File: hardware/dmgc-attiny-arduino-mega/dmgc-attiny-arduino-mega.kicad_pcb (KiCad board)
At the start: 2 copper layers, 101.6 x 53.3 mm, 34 parts, among them J1 Power, J2 PWM, J3 Analog, J4 PWM, J5 Analog, J6 Communication, J7 Digital, SW1 PUSH, SW2 LEFT, SW3 RIGHT, SW4 SELECT, SW5 START/RESET, U1 ATtiny85-20P

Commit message: Updated arduino shield, start implementing a multiplexer to switch from flashing the attiny85 to running the attiny85.
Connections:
- D8 pad 4: unconnected-(D8-Pad4) -> GND
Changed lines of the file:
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@@
   (net 85 "Net-(D6-Pad4)")
   (net 86 "Net-(D7-Pad4)")
-  (net 87 "unconnected-(D8-Pad4)")
+  (net 87 "Net-(U1-Pad1)")
   (net 88 "Net-(R1-Pad2)")
   (net 89 "Net-(R2-Pad2)")
@@
   (net 96 "Net-(SW4-Pad1)")
   (net 97 "Net-(SW5-Pad1)")
-  (net 98 "Net-(R6-Pad2)")
-  (net 99 "unconnected-(SW1-Pad4)")
-  (net 100 "unconnected-(SW2-Pad4)")
-  (net 101 "unconnected-(SW3-Pad4)")
-  (net 102 "unconnected-(SW4-Pad4)")
-  (net 103 "unconnected-(SW5-Pad4)")
+  (net 98 "unconnected-(SW1-Pad4)")
+  (net 99 "unconnected-(SW2-Pad4)")
+  (net 100 "unconnected-(SW3-Pad4)")
+  (net 101 "unconnected-(SW4-Pad4)")
+  (net 102 "unconnected-(SW5-Pad4)")
   (footprint "Connector_PinSocket_2.54mm:PinSocket_2x18_P2.54mm_Vertical" locked (layer "F.Cu")
     (at 193.98 92.38 180)
@@
       (effects (font (size 1 1) (thickness 0.15)))
     )
+    (fp_line (start -3.87 -1.33) (end -3.868838 43.122722) (layer "F.SilkS") (width 0.12))
     (fp_line (start -1.27 -1.33) (end -1.27 1.27) (layer "F.SilkS") (width 0.12))
     (fp_line (start 1.33 1.27) (end 1.33 44.51) (layer "F.SilkS") (width 0.12))
@@
     (fp_line (start -1.27 1.27) (end 1.33 1.27) (layer "F.SilkS") (width 0.12))
     (fp_line (start 1.33 -1.33) (end 1.33 0) (layer "F.SilkS") (width 0.12))
-    (fp_line (start -3.87 44.51) (end 1.33 44.51) (layer "F.SilkS") (width 0.12))
     (fp_line (start -3.87 -1.33) (end -1.27 -1.33) (layer "F.SilkS") (width 0.12))
-    (fp_line (start -3.87 -1.33) (end -3.87 44.51) (layer "F.SilkS") (width 0.12))
+    (fp_line (start 1.33 44.51) (end -2.536649 44.510068) (layer "F.SilkS") (width 0.12))
+    (fp_arc (start -2.536649 44.510068) (mid -3.499381 44.101239) (end -3.868838 43.122722) (layer "F.SilkS") (width 0.12))
     (fp_line (start -4.34 -1.8) (end 1.76 -1.8) (layer "F.CrtYd") (width 0.05))
     (fp_line (start -4.34 44.95) (end -4.34 -1.8) (layer "F.CrtYd") (width 0.05))
@@
       (net 1 "GND") (pinfunction "3") (pintype "passive"))
     (pad "4" thru_hole circle (at 6.5 4.5 90) (size 2 2) (drill 1.1) (layers *.Cu *.Mask)
-      (net 100 "unconnected-(SW2-Pad4)") (pinfunction "4") (pintype "passive"))
+      (net 99 "unconnected-(SW2-Pad4)") (pinfunction "4") (pintype "passive"))
     (model "${KICAD6_3DMODEL_DIR}/Button_Switch_THT.3dshapes/SW_PUSH_6mm.wrl"
       (offset (xyz 0 0 0))
@@
       (net 1 "GND") (pinfunction "3") (pintype "passive"))
     (pad "4" thru_hole circle (at 6.5 4.5 90) (size 2 2) (drill 1.1) (layers *.Cu *.Mask)
-      (net 99 "unconnected-(SW1-Pad4)") (pinfunction "4") (pintype "passive"))
+      (net 98 "unconnected-(SW1-Pad4)") (pinfunction "4") (pintype "passive"))
     (model "${KICAD6_3DMODEL_DIR}/Button_Switch_THT.3dshapes/SW_PUSH_6mm.wrl"
       (offset (xyz 0 0 0))
@@
       (net 1 "GND") (pinfunction "3") (pintype "passive"))
     (pad "4" thru_hole circle (at 6.5 4.5 90) (size 2 2) (drill 1.1) (layers *.Cu *.Mask)
-      (net 102 "unconnected-(SW4-Pad4)") (pinfunction "4") (pintype "passive"))
+      (net 101 "unconnected-(SW4-Pad4)") (pinfunction "4") (pintype "passive"))
     (model "${KICAD6_3DMODEL_DIR}/Button_Switch_THT.3dshapes/SW_PUSH_6mm.wrl"
       (offset (xyz 0 0 0))
@@
       (net 1 "GND") (pinfunction "3") (pintype "passive"))
     (pad "4" thru_hole circle (at 6.5 4.5 90) (size 2 2) (drill 1.1) (layers *.Cu *.Mask)
-      (net 103 "unconnected-(SW5-Pad4)") (pinfunction "4") (pintype "passive"))
+      (net 102 "unconnected-(SW5-Pad4)") (pinfunction "4") (pintype "passive"))
     (model "${KICAD6_3DMODEL_DIR}/Button_Switch_THT.3dshapes/SW_PUSH_6mm.wrl"
       (offset (xyz 0 0 0))
@@
       (net 1 "GND") (pinfunction "3") (pintype "passive"))
     (pad "4" thru_hole circle (at 6.5 4.5 90) (size 2 2) (drill 1.1) (layers *.Cu *.Mask)
-      (net 101 "unconnected-(SW3-Pad4)") (pinfunction "4") (pintype "passive"))
+      (net 100 "unconnected-(SW3-Pad4)") (pinfunction "4") (pintype "passive"))
     (model "${KICAD6_3DMODEL_DIR}/Button_Switch_THT.3dshapes/SW_PUSH_6mm.wrl"
       (offset (xyz 0 0 0))
@@
       (net 79 "Net-(D1-Pad2)") (pintype "passive"))
     (pad "2" smd roundrect (at 0.32 0 270) (size 0.46 0.4) (layers "F.Cu" "F.Mask") (roundrect_rratio 0.25)
-      (net 98 "Net-(R6-Pad2)") (pintype "passive"))
+      (net 87 "Net-(U1-Pad1)") (pintype "passive"))
     (model "${KICAD6_3DMODEL_DIR}/Resistor_SMD.3dshapes/R_0201_0603Metric.wrl"
       (offset (xyz 0 0 0))
@@
     (fp_line (start 0.635 8.89) (end 0.635 -0.27) (layer "F.Fab") (width 0.1))
     (pad "1" thru_hole rect (at 0 0) (size 1.6 1.6) (drill 0.8) (layers *.Cu *.Mask)
-      (net 98 "Net-(R6-Pad2)") (pinfunction "~{RESET}/PB5") (pintype "bidirectional"))
+      (net 87 "Net-(U1-Pad1)") (pinfunction "~{RESET}/PB5") (pintype "bidirectional"))
     (pad "2" thru_hole oval (at 0 2.54) (size 1.6 1.6) (drill 0.8) (layers *.Cu *.Mask)
       (net 96 "Net-(SW4-Pad1)") (pinfunction "XTAL1/PB3") (pintype "bidirectional"))
@@
       (net 34 "+5V") (pinfunction "VDD") (pintype "power_in"))
     (pad "4" smd rect (at 2.45 -1.6) (size 1.5 1) (layers "F.Cu" "F.Paste" "F.Mask")
-      (net 87 "unconnected-(D8-Pad4)") (pinfunction "DO") (pintype "output"))
+      (net 1 "GND") (pinfunction "DO") (pintype "output"))
     (model "${KICAD6_3DMODEL_DIR}/LED_SMD.3dshapes/LED_Inolux_IN-PI554FCH_PLCC4_5.0x5.0mm_P3.2mm.wrl"
       (offset (xyz 0 0 0))
@@
   (segment (start 161.53 60.02) (end 160.87 59.36) (width 0.25) (layer "F.Cu") (net 86))
   (segment (start 168.76 60.02) (end 161.53 60.02) (width 0.25) (layer "F.Cu") (net 86))
+  (segment (start 174.94 64.652231) (end 174.948637 64.643594) (width 0.25) (layer "F.Cu") (net 87))
+  (segment (start 174.94 68.26) (end 174.94 64.652231) (width 0.25) (layer "F.Cu") (net 87))
   (segment (start 136.27 85.98591) (end 136.27 87.59) (width 0.25) (layer "F.Cu") (net 88))
   (segment (start 137.25269 85.00322) (end 136.27 85.98591) (width 0.25) (layer "F.Cu") (net 88))
@@
   (segment (start 176.528198 69.848198) (end 181.525606 64.85079) (width 0.25) (layer "F.Cu") (net 97))
   (segment (start 188.45 64.94522) (end 188.45 84.573604) (width 0.25) (layer "F.Cu") (net 97))
-  (segment (start 174.94 64.652231) (end 174.948637 64.643594) (width 0.25) (layer "F.Cu") (net 98))
-  (segment (start 174.94 68.26) (end 174.94 64.652231) (width 0.25) (layer "F.Cu") (net 98))
   (zone (net 34) (net_name "+5V") (layer "F.Cu") (hatch edge 0.508)
     (connect_pads (clearance 0.508))

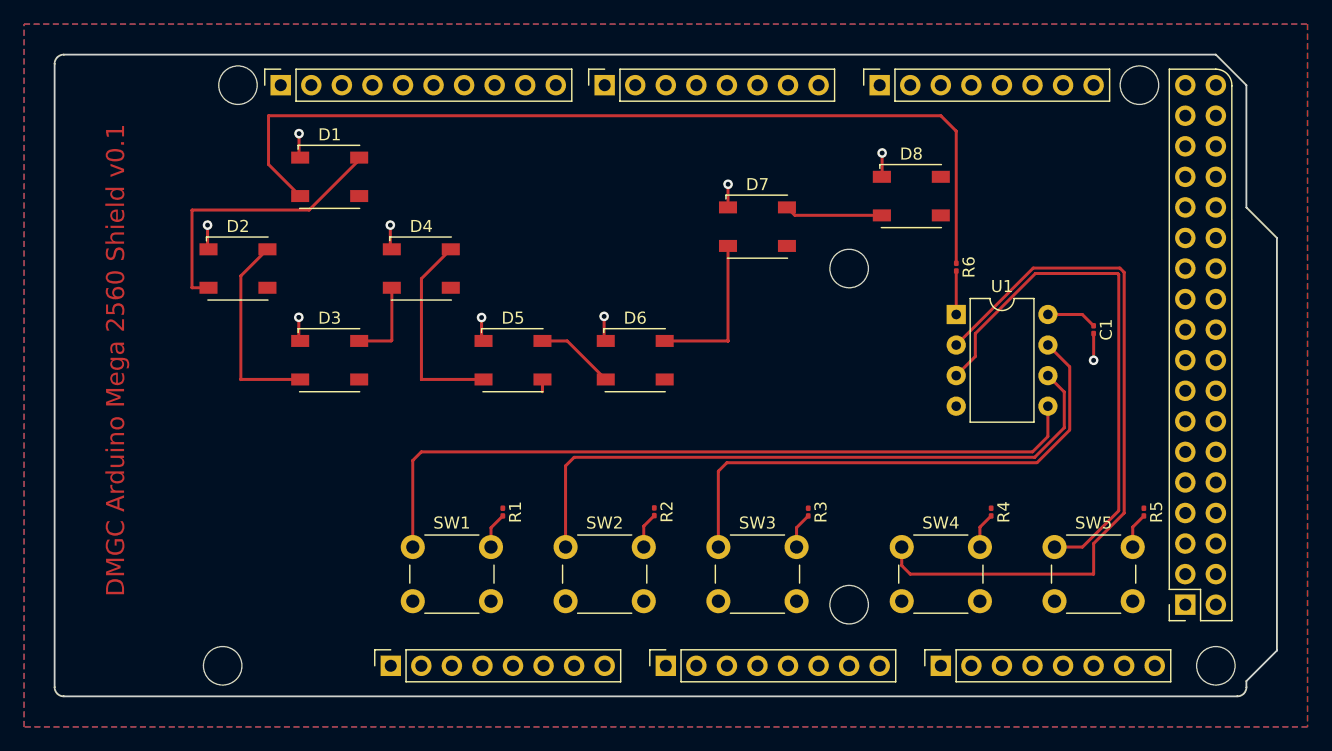
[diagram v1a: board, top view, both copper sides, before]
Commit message: Updated arduino shield to include switching circuit for flashing and running.
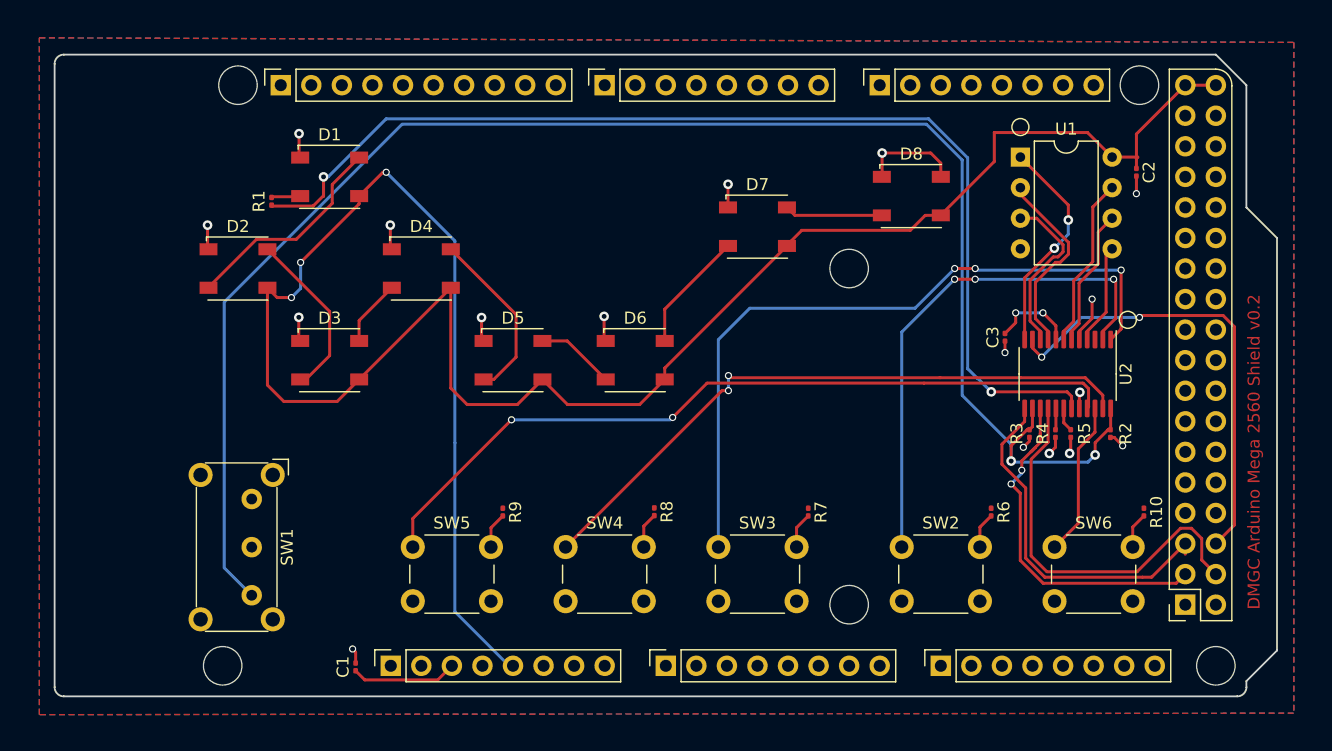
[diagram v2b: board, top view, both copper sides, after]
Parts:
- added C1: 10uf, Capacitor_SMD:C_0201_0603Metric, F.Cu at (125.0, 97.6)
- added C3: 100n, Capacitor_SMD:C_0201_0603Metric, F.Cu at (179.0, 70.2)
- added G***: LOGO, juvinious:logo, B.Cu at (109.5, 72.7)
- added R2: 4.7k, Resistor_SMD:R_0201_0603Metric, F.Cu at (187.8, 78.2)
- added R3: 4.7k, Resistor_SMD:R_0201_0603Metric, F.Cu at (181.0, 78.2)
- added R4: 50, Resistor_SMD:R_0201_0603Metric, F.Cu at (183.2, 78.2)
- added R5: 50, Resistor_SMD:R_0201_0603Metric, F.Cu at (184.5, 78.2)
- added SW1: Toggle Flash / Run, Button_Switch_THT:SW_E-Switch_EG1224_SPDT_Angled, F.Cu at (116.4, 83.6)
- added U2: Mutex, Package_SO:TSSOP-24_4.4x7.8mm_P0.65mm, F.Cu at (184.2, 73.2)
- moved R1 57.2 mm to (118.0, 58.9), turned to 90 degrees
- moved U1 14.1 mm to (180.3, 55.2)
- moved C2 13.6 mm to (189.9, 56.4)
- renumbered C1 to C2, J3 to J2, J5 to J3, J7 to J4, J2 to J5, J4 to J6, J6 to J7, R6 to R1, R5 to R10, R4 to R6, R3 to R7, R2 to R8, R1 to R9, SW4 to SW2, SW2 to SW4, SW1 to SW5, SW5 to SW6
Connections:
- J4 pad 3: /*52 -> SCK
- J4 pad 4: /53 -> SS
- J4 pad 5: /50 -> MISO
- J4 pad 6: /51 -> MOSI
- R1 pad 1: Net-(D1-Pad2) -> LED_CTRL
- R1 pad 2: Net-(U1-Pad1) -> Net-(D1-Pad2)
- R10 pad 1: +5V -> +3V3
- R6 pad 1: +5V -> +3V3
- R7 pad 1: +5V -> +3V3
- R8 pad 1: +5V -> +3V3
- R9 pad 1: +5V -> +3V3
- SW2 pad 1: Net-(SW4-Pad1) -> /NC_PB0
- SW3 pad 1: Net-(SW3-Pad1) -> /NC_PB1
- SW4 pad 1: Net-(SW2-Pad1) -> /NC_PB2
- SW5 pad 1: Net-(SW1-Pad1) -> /NC_PB3
- SW6 pad 1: Net-(SW5-Pad1) -> /NC_PB5
- U1 pad 1: Net-(U1-Pad1) -> /COM_PB5
- U1 pad 2: Net-(SW4-Pad1) -> /COM_PB3
- U1 pad 3: Net-(SW5-Pad1) -> /COM_PB4
- U1 pad 5: Net-(SW1-Pad1) -> /COM_PB0
- U1 pad 6: Net-(SW2-Pad1) -> /COM_PB1
- U1 pad 7: Net-(SW3-Pad1) -> /COM_PB2
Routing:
- net +5V: track 5.22 -> 180.9 mm, vias 0 -> 3
- net Net-(R2-Pad2): track 0.00 -> 137.7 mm, vias 0 -> 2
- net LED_CTRL: track 0.00 -> 92.9 mm, vias 0 -> 2
- net Net-(D1-Pad2): track 76.4 -> 2.39 mm
- net /NC_PB3: track 0.00 -> 65.1 mm, vias 0 -> 2
- net Net-(SW1-Pad1): track 63.3 -> 0.00 mm
- net Net-(SW4-Pad1): track 60.7 -> 0.00 mm
- net /NC_PB1: track 0.00 -> 59.3 mm, vias 0 -> 3
- net Net-(SW2-Pad1): track 54.4 -> 0.00 mm
- net /NC_PB2: track 0.00 -> 53.1 mm, vias 0 -> 2
- net Net-(SW3-Pad1): track 44.7 -> 0.00 mm
- net Net-(SW5-Pad1): track 44.4 -> 0.00 mm
- net /NC_PB0: track 0.00 -> 42.8 mm, vias 0 -> 3
- net MOSI: track 0.00 -> 38.3 mm, vias 0 -> 2
- net SS: track 0.00 -> 32.9 mm
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- added copper zone on F.Cu, net +3V3
- removed copper zone on F.Cu, net +5V
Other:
- board text added: "DMGC Arduino Mega 2560 Shield v0.2"
- board text removed: "DMGC Arduino Mega 2560 Shield v0.1"

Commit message: Updated arduino shield routing and fixed pcb issues.
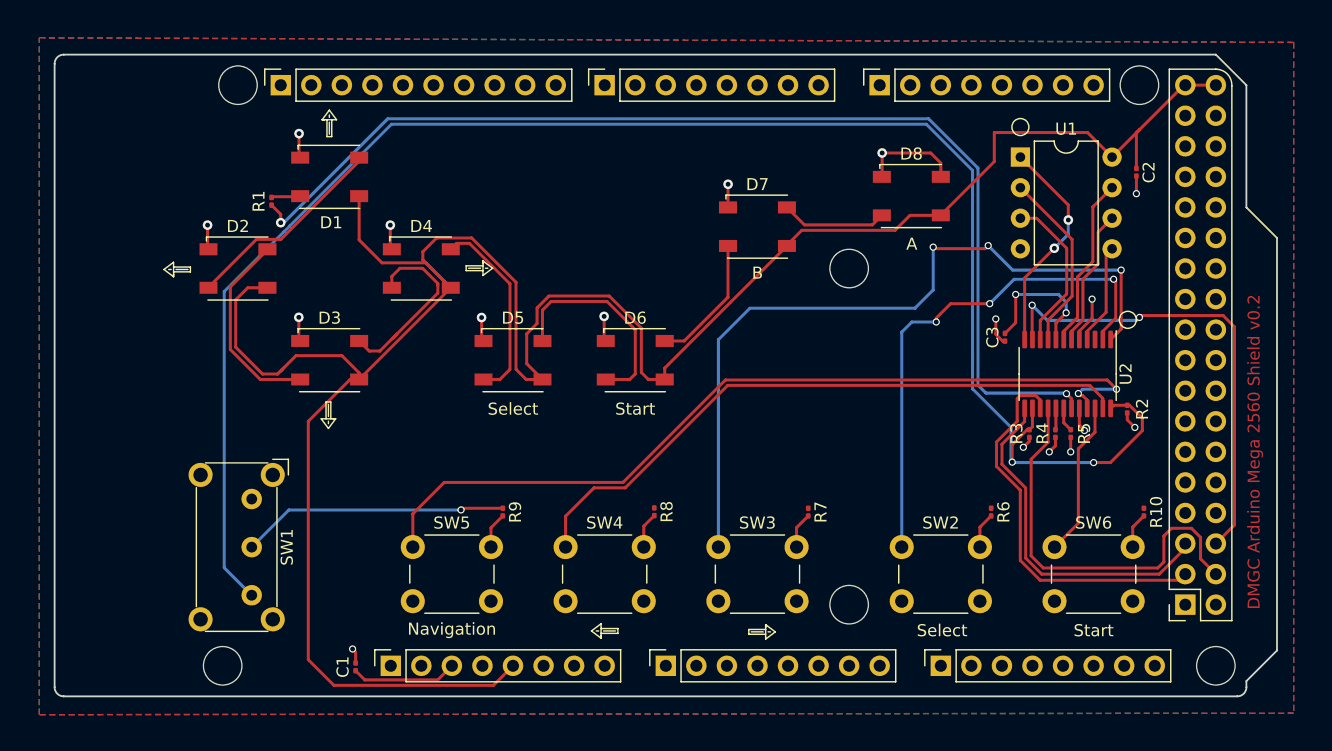
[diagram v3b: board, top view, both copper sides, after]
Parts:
- removed the G*** at (109.5, 72.7)
- added G***: logo-only, juvinious:logo-only, F.Cu at (106.5, 50.1)
- added G***: name, juvinious:name, B.Cu at (103.0, 63.3)
- added arrow**: Up, juvinious:Arrow, F.Cu at (125.8, 52.5)
- added arrow**: Left, juvinious:Arrow, F.Cu at (110.3, 61.5)
- added arrow**: Down, juvinious:Arrow, F.Cu at (119.8, 76.5)
- added arrow**: Left, juvinious:Arrow, F.Cu at (145.8, 91.6)
- added arrow**: Right, juvinious:Arrow, F.Cu at (135.2, 67.4)
- added arrow**: Left, juvinious:Arrow, F.Cu at (158.7, 97.6)
- moved R2 2.47 mm to (189.2, 76.1)
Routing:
- net +3V3: track 7.01 -> 33.7 mm, vias 2 -> 3
- net +5V: track 180.9 -> 198.2 mm, vias 3 -> 0
- net Net-(D5-Pad4): track 6.59 -> 17.9 mm
- net Net-(D3-Pad4): track 5.55 -> 15.8 mm
- net Net-(R2-Pad2): track 137.7 -> 145.1 mm
- net /NC_PB3: track 65.1 -> 71.2 mm
- net /NC_PB1: track 59.3 -> 63.1 mm
- net SCK: track 29.5 -> 32.5 mm, vias 2 -> 0
- net Net-(D2-Pad4): track 14.3 -> 16.9 mm
- net GND: track 36.6 -> 38.5 mm
- net Net-(D4-Pad4): track 14.7 -> 16.2 mm
- net MOSI: track 38.3 -> 39.4 mm
- net SS: track 32.9 -> 33.9 mm
- net Net-(D6-Pad4): track 10.1 -> 11.0 mm
- net LED_CTRL: track 92.9 -> 92.1 mm
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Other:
- board text added: "A"
- board text added: "B"
- board text added: "Navigation"
- board text added: "Select"
- board text added: "Start"

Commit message: Updated gerbers to v0.3, fixed 0603 footprints.
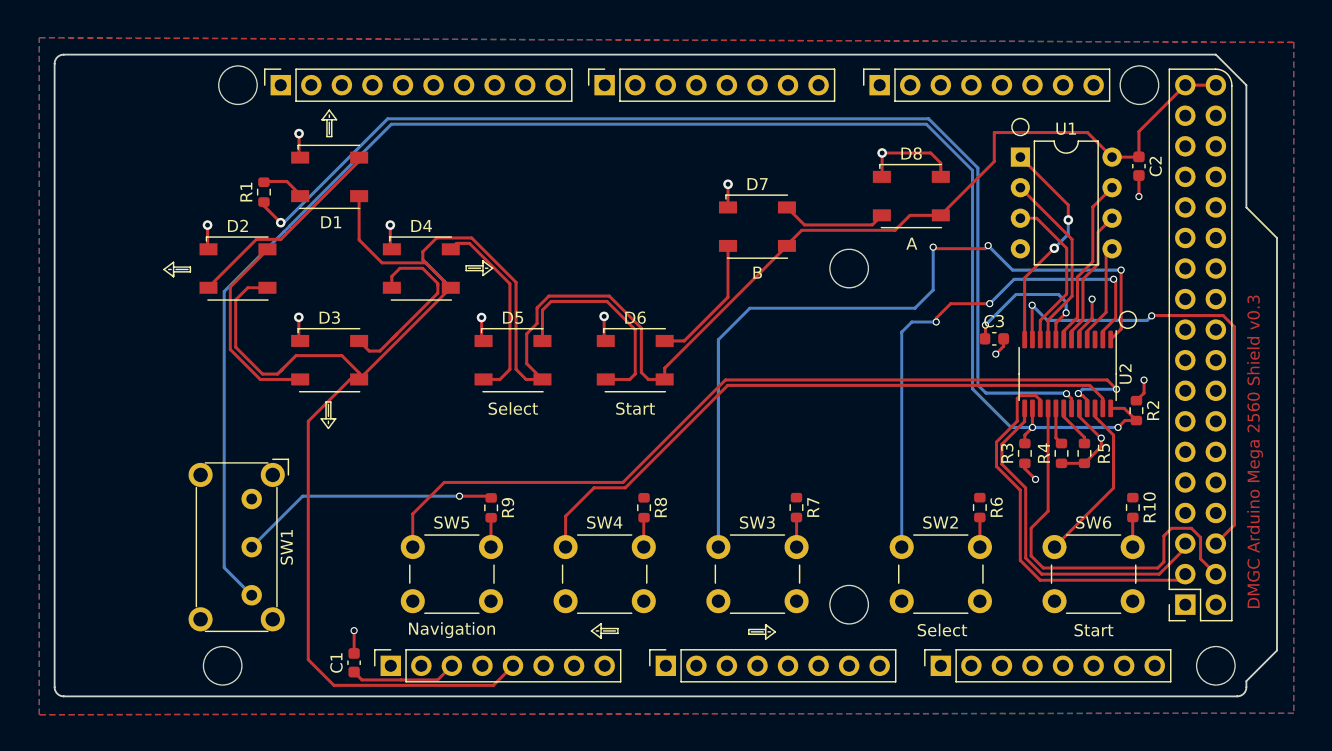
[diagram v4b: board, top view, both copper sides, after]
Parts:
- C1, C2, C3: footprint Capacitor_SMD:C_0201_0603Metric -> Capacitor_SMD:C_0603_1608Metric
- R1, R10, R2, R3, R4, R5, R6, R7, R8, R9: footprint Resistor_SMD:R_0201_0603Metric -> Resistor_SMD:R_0603_1608Metric
- moved R5 2.01 mm to (185.6, 79.8)
- moved R4 1.73 mm to (183.7, 79.8)
- moved R3 1.69 mm to (180.6, 79.8)
- moved R7 1.05 mm to (161.7, 84.3)
- moved R9 1.03 mm to (136.3, 84.3)
- moved R6 1.01 mm to (176.9, 84.3)
- moved R10 0.99 mm to (189.6, 84.3)
- moved R1 0.99 mm to (117.4, 58.1)
- moved R8 0.92 mm to (149.0, 84.3)
- moved C3 0.90 mm to (178.1, 70.3), turned to 0 degrees
- moved R2 0.77 mm to (189.9, 76.3), turned to -90 degrees
- moved C2 0.55 mm to (190.1, 55.9)
- moved C1 0.37 mm to (124.9, 97.2)
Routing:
- net Net-(R2-Pad2): track 145.1 -> 135.8 mm
- net GND: track 38.5 -> 43.0 mm, vias 17 -> 15
- net +5V: track 198.2 -> 196.2 mm
- net /NO_PB4: track 2.01 -> 3.63 mm
- net Net-(D1-Pad2): track 2.39 -> 3.72 mm
- net /NO_PB3: track 1.79 -> 3.11 mm
- net /NC_PB5: track 12.9 -> 14.2 mm
- net +3V3: track 33.7 -> 34.4 mm
- net Net-(R9-Pad2): track 2.99 -> 2.44 mm
- net Net-(R7-Pad2): track 2.99 -> 2.46 mm
- net Net-(R8-Pad2): track 2.97 -> 2.45 mm
- net LED_CTRL: track 92.1 -> 92.6 mm
- net Net-(R6-Pad2): track 2.97 -> 2.46 mm
- net Net-(R10-Pad2): track 2.97 -> 2.46 mm
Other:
- board text added: "DMGC Arduino Mega 2560 Shield v0.3"
- board text removed: "DMGC Arduino Mega 2560 Shield v0.2"
